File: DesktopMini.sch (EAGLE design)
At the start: 38 parts, among them J1 CONN_82.54_SCREW, J2 CONN_3, U1 ADS1115, U2 ATMEGA328P_TQFP, U3 SN74LVC1G17DCK, U4 FT232RL, U5 MIC2091, U6 MIC53653.3SC70, Y1 16MHz

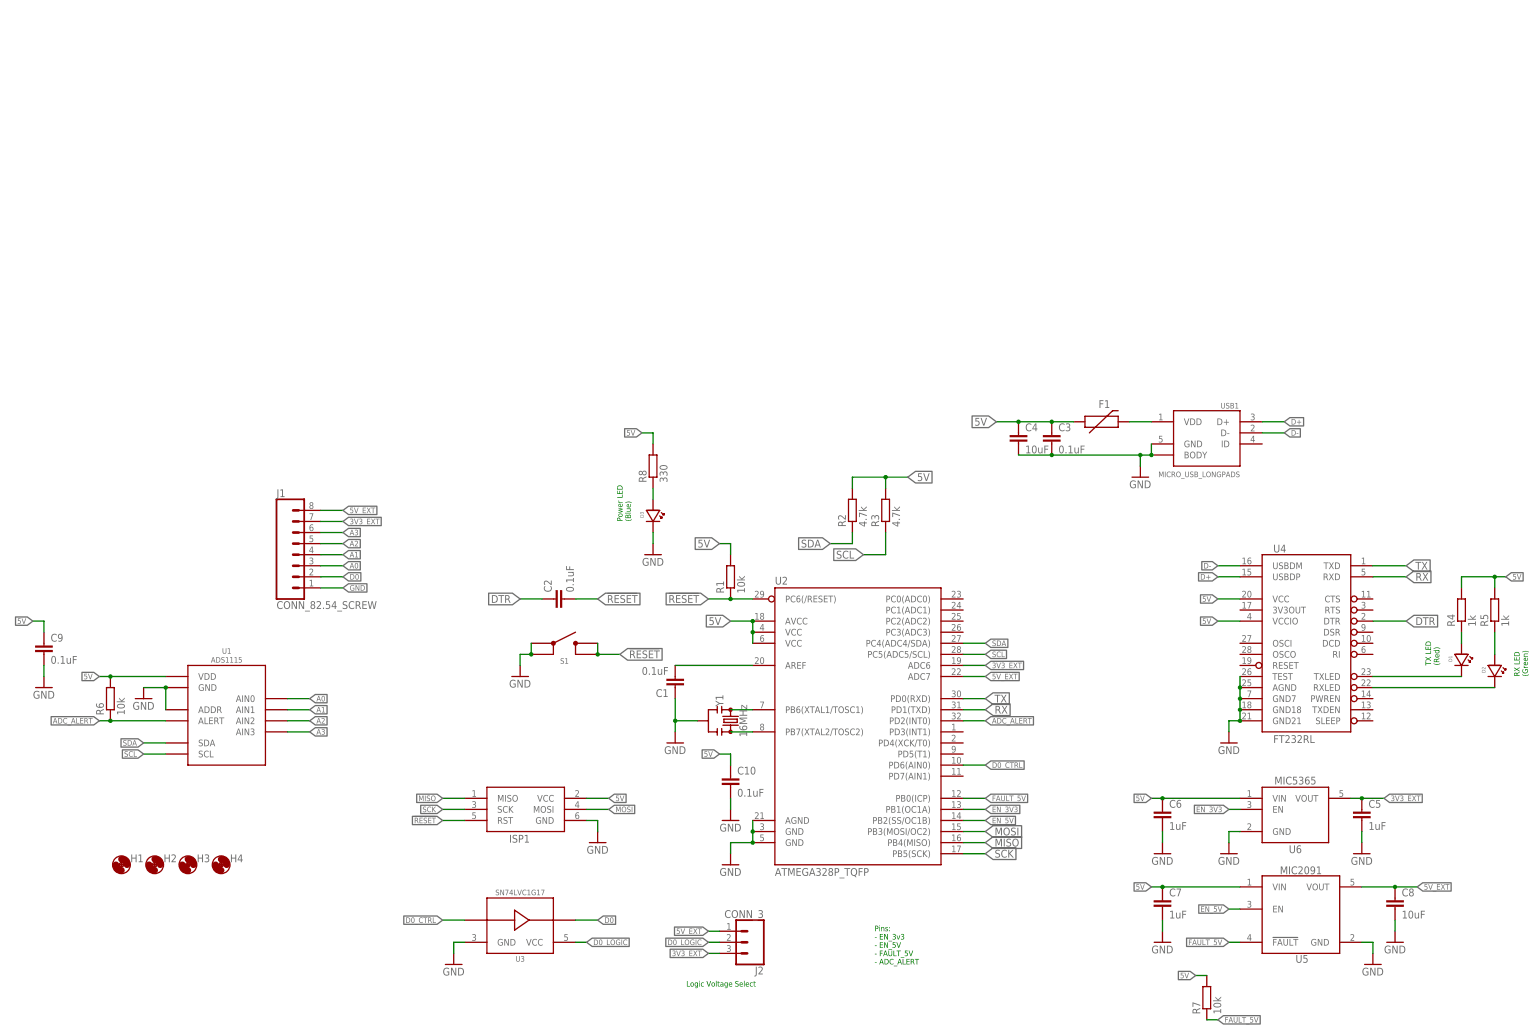
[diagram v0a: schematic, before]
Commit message: Minor updates, v0.0 to fab
Added auxiliary LED and did minor cleanup, added BMP image via script
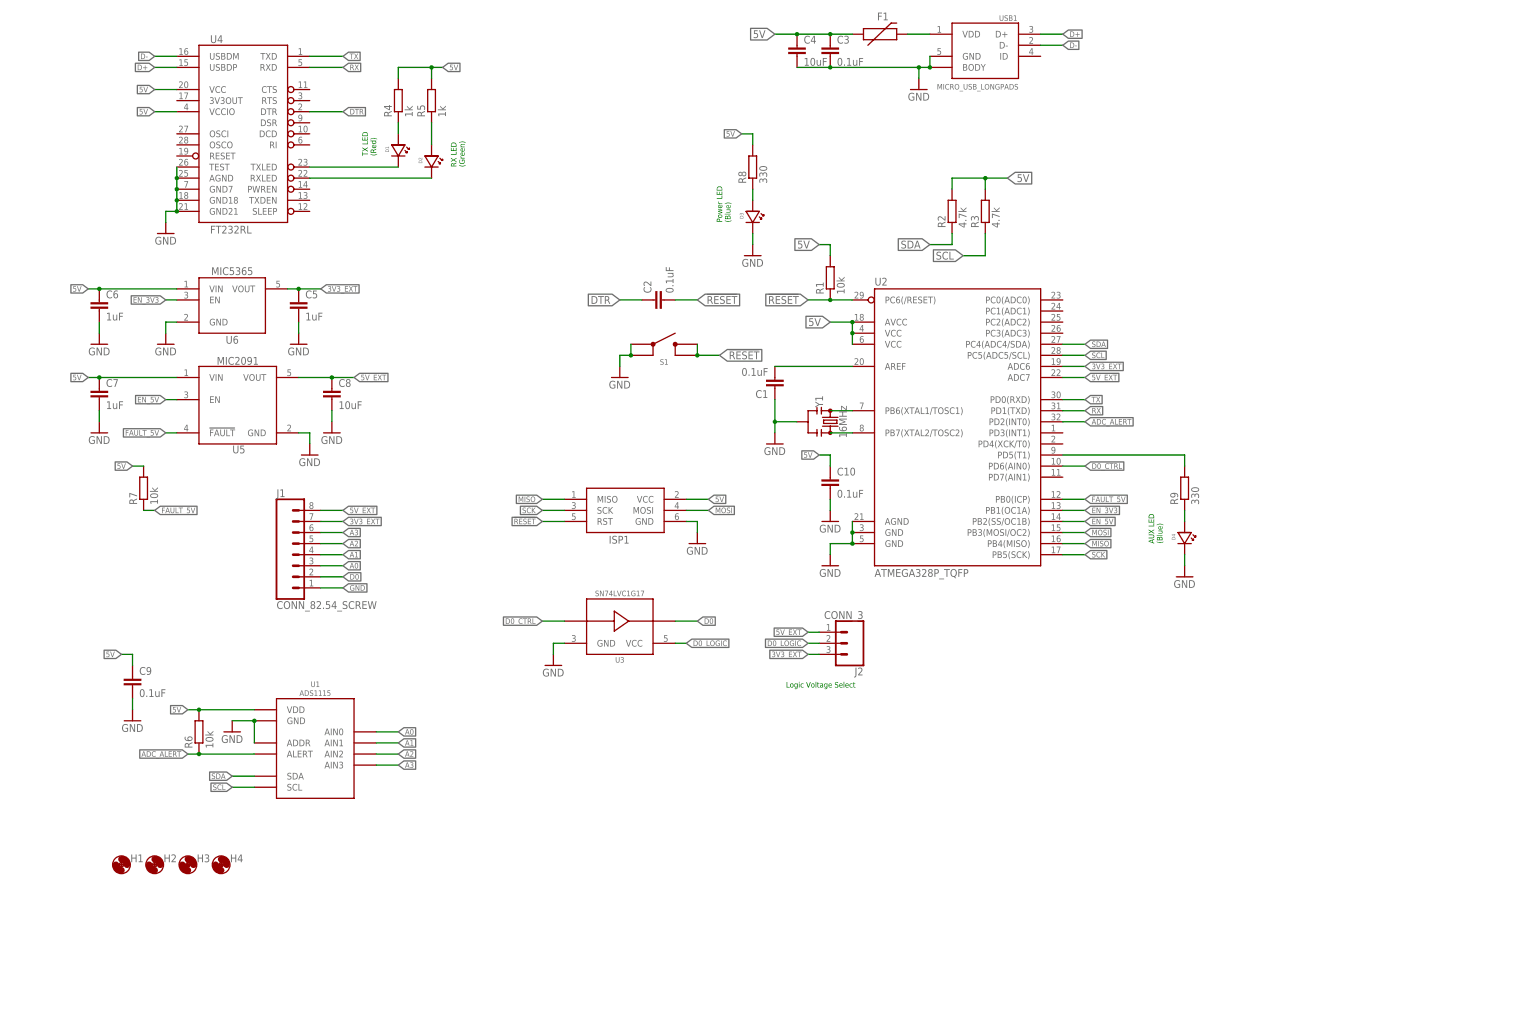
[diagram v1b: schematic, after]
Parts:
- added D4: LEDBLUE0603, bschulz:LEDBLUE0603
- added R9: 330, bschulz_passives:R-EU_330R0603
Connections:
- new net AUX_LED: R9.2, U2.PD5(T1)
- new net N$11: D4.ANODE, R9.1
- net GND: now also D4.CATHODE
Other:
- note added: "AUX LED (Blue)"
- note removed: "Pins: - EN_3v3 - EN_5V - FAULT_5V - ADC_ALERT"
- moved on the sheet: C1, C10, C2, C3, C4, C5, C6, C7, C8, C9, D1, D2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
